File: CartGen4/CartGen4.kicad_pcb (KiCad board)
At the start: 4 copper layers, 52.8 x 60.9 mm, 77 parts, among them J1 MEM2080-00-128-00-A, SW1 SW_Push, U1 TPS65266-1RHBR, U10 IS25WP080D-JNLE, U11 DS1391U-33+, U2 SN74LV1T34DCKR, U3 SIT8008BI-73-33E-33.333333G, U4 NXS0108BQX, U5 AS1C8M16PL-70BIN, U6 NXS0108BQX, U7 NXS0108BQX, U8 NXS0104BQX, U9 LFXP2-8E-5MN132C, Y1 FC-135R 32.7680KA-E5

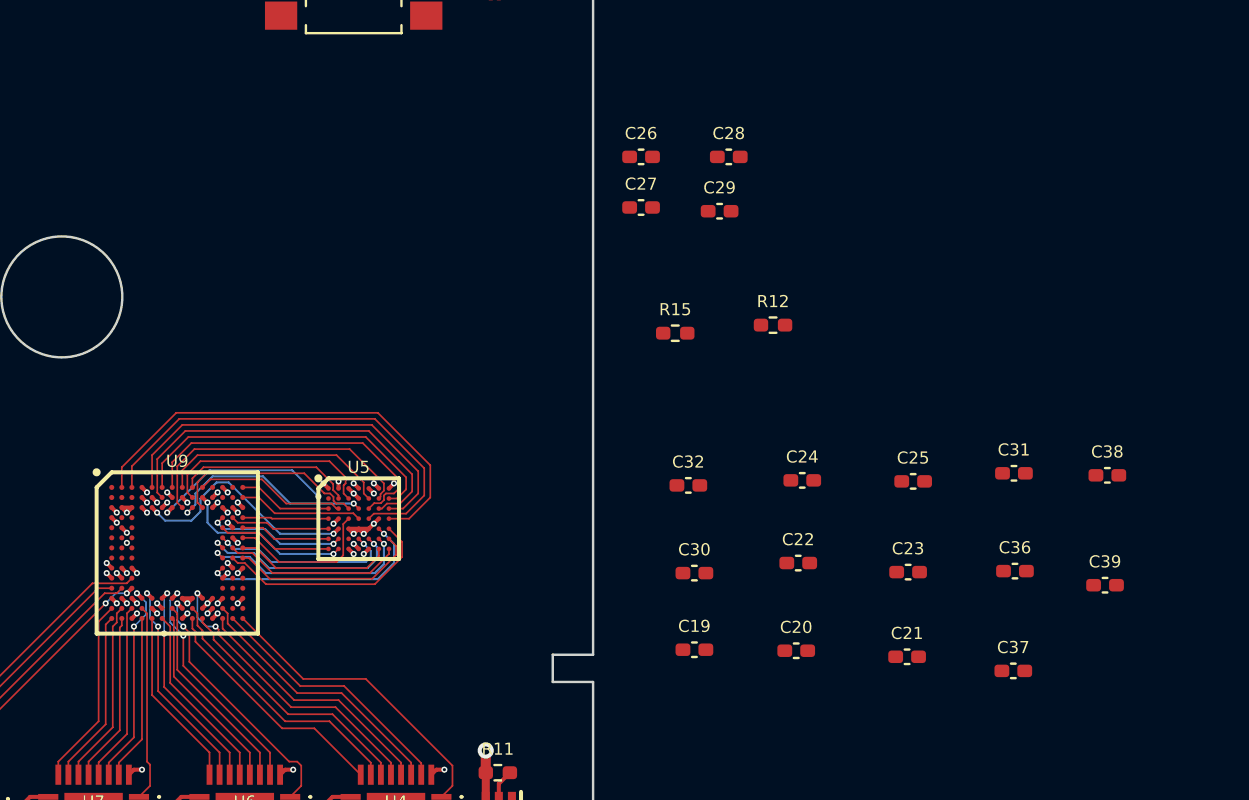
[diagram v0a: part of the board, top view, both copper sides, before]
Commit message: Added RAM decoupling capacitors
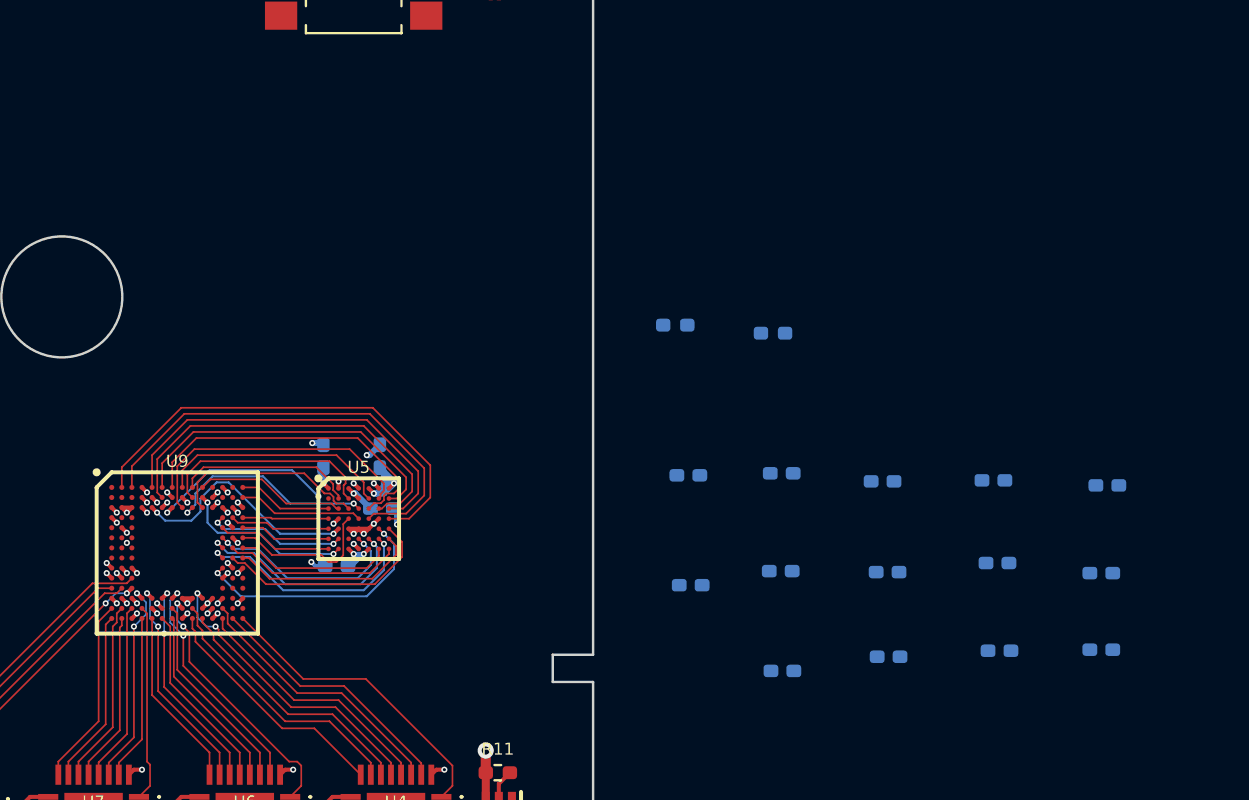
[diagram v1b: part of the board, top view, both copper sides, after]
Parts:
- C19, C20, C21, C22, C23, C24, C25, C26, C27, C28, C29, C30, C31, C32, C36, C37, C38, C39, R12, R15: moved to B.Cu
- moved C29 25.9 mm to (79.7, 74.3), turned to 180 degrees
- moved C28 22.8 mm to (81.8, 68.8), turned to 90 degrees
- moved C26 21.7 mm to (81.9, 71.5)
- moved C32 20.8 mm to (117.9, 70.3), turned to 180 degrees
- moved C38 20.8 mm to (97.1, 69.8), turned to 180 degrees
- moved C39 20.6 mm to (97.2, 75.2), turned to 180 degrees
- moved C19 20.2 mm to (117.6, 78.5), turned to 180 degrees
- moved C30 20.2 mm to (117.6, 74.7), turned to 180 degrees
- moved C27 20.0 mm to (79.0, 68.8), turned to 90 degrees
- moved C36 11.6 mm to (101.7, 74.5), turned to 180 degrees
- moved C31 11.5 mm to (101.7, 69.7), turned to 180 degrees
- moved C37 11.5 mm to (101.8, 79.5), turned to 180 degrees
- moved C20 10.1 mm to (112.5, 78.5), turned to 180 degrees
- moved C22 9.88 mm to (112.4, 74.2), turned to 180 degrees
- moved C24 9.48 mm to (112.2, 70.0), turned to 180 degrees
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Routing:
- net +1V8: track 20.9 -> 29.4 mm
- net GND: track 81.4 -> 84.4 mm, vias 48 -> 52
- net RAM_CE1#: track 10.1 -> 11.0 mm
- net RAM_CRE: track 9.12 -> 10.0 mm
- net RAM_LB#: track 10.6 -> 11.4 mm
- net RAM_UB#: track 11.6 -> 12.4 mm

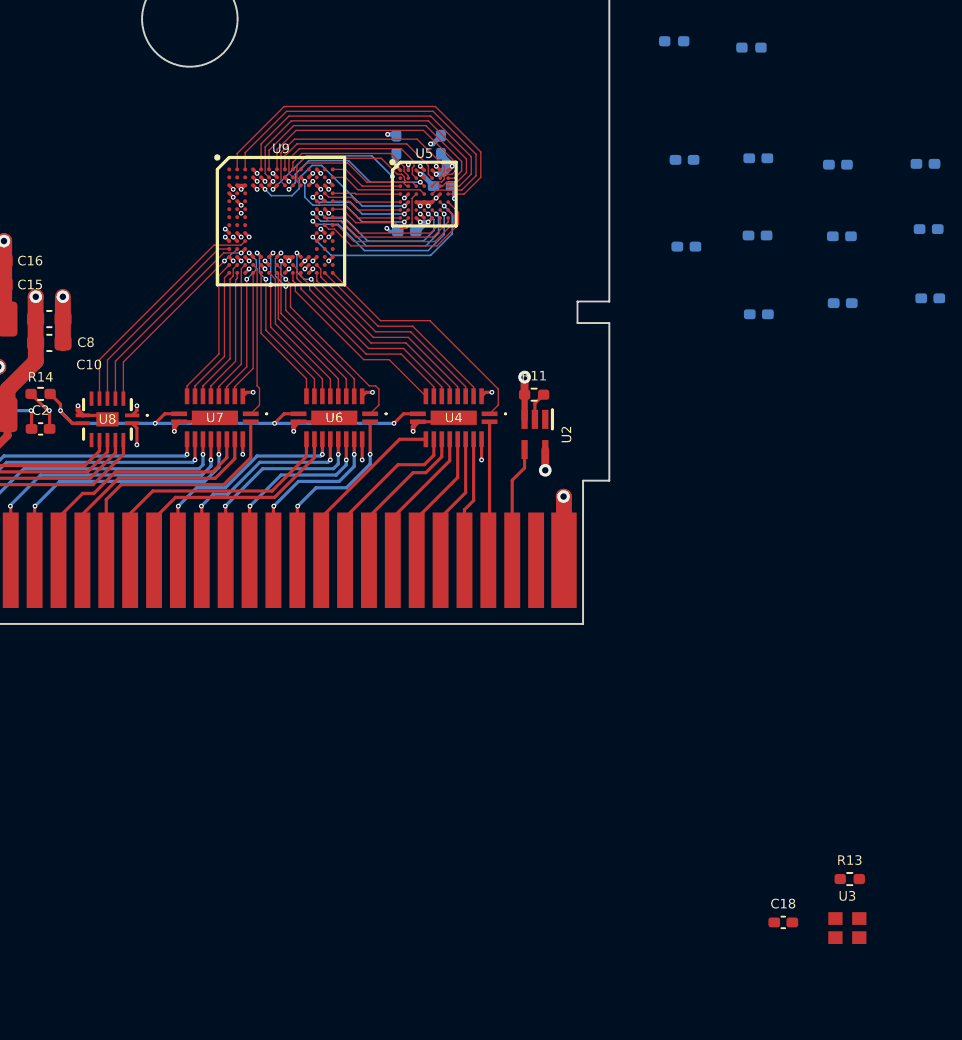
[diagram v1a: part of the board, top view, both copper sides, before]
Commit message: Connected FPGA ref clock
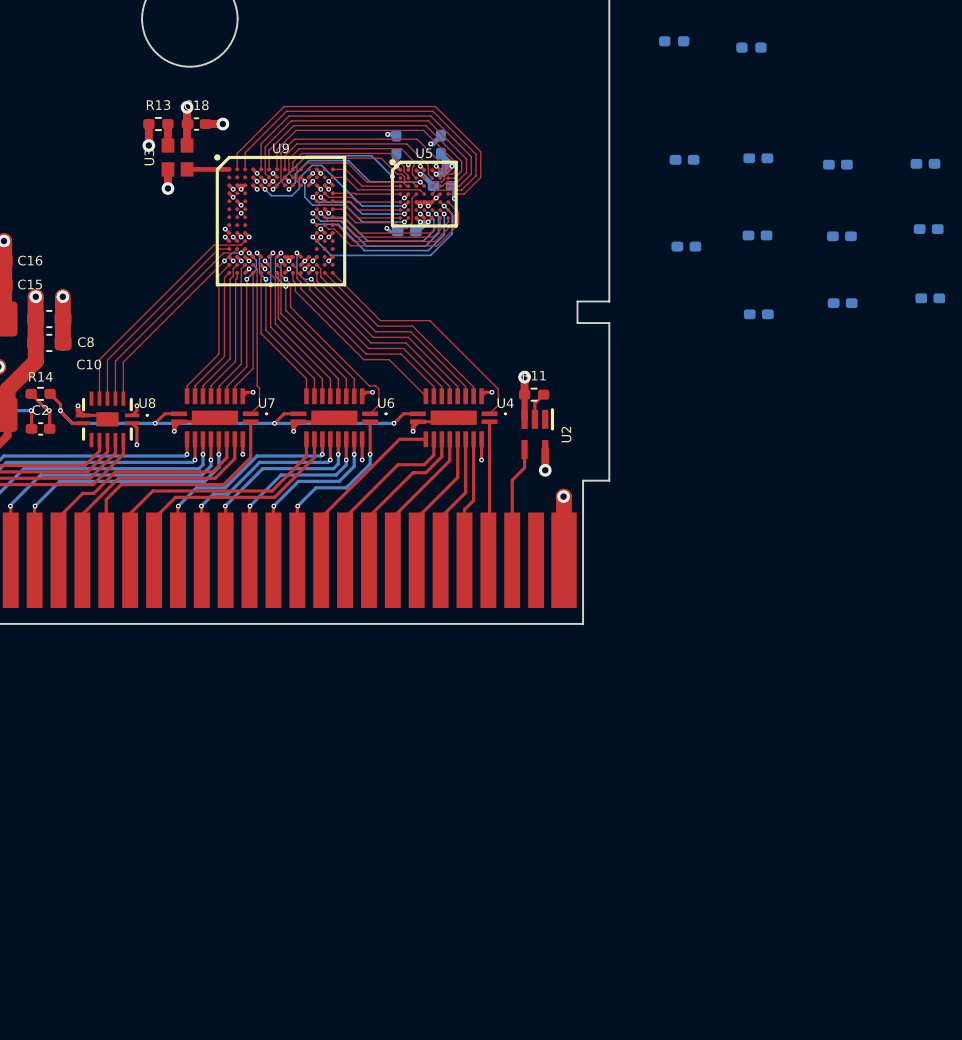
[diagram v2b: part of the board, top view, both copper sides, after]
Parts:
- moved R13 64.3 mm to (64.0, 67.5)
- moved U3 64.1 mm to (65.2, 69.7), turned to -90 degrees
- moved C18 62.2 mm to (66.5, 67.5)
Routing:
- net +1V8: track 29.4 -> 33.1 mm, vias 12 -> 14
- net FPGA_CLK33M: track 0.00 -> 2.65 mm
- net GND: track 84.4 -> 86.7 mm, vias 52 -> 54
- net Net-(R13-Pad2): track 0.00 -> 1.35 mm
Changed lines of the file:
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@@
   )
   (footprint "Resistor_SMD:R_0402_1005Metric_Pad0.72x0.64mm_HandSolder" (layer "F.Cu")
-    (at 107.475 114.975)
+    (at 64.05 67.55)
     (descr "Resistor SMD 0402 (1005 Metric), square (rectangular) end terminal, IPC_7351 nominal with elongated pad for handsoldering. (Body size source: IPC-SM-782 page 72, https://www.pcb-3d.com/wordpress/wp-content/uploads/ipc-sm-782a_amendment_1_and_2.pdf), generated with kicad-footprint-generator")
     (tags "resistor handsolder")
@@
   )
   (footprint "SamacSys_Parts:SIT8008BI-73-33E-33.333333G" (layer "F.Cu")
-    (at 107.325 118.055)
+    (at 65.25 69.65 -90)
     (property "Critical" "Y")
     (property "Description" "Standard Clock Oscillators -40 to 85C, 2016, 50ppm, 3.3V, 33.333333MHz, OE, 250 pcs T&R 8 mm")
@@
     (property "Source" "SPEC")
     (attr smd)
-    (fp_text reference "U3" (at 0 -2 unlocked) (layer "F.SilkS")
+    (fp_text reference "U3" (at 0 1.75 90 unlocked) (layer "F.SilkS")
       (effects (font (size 0.6 0.6) (thickness 0.125)))
     )
-    (fp_text value "SIT8008BI-73-33E-33.333333G" (at 0 -5.45 unlocked) (layer "F.Fab")
+    (fp_text value "SIT8008BI-73-33E-33.333333G" (at 0 -5.45 -90 unlocked) (layer "F.Fab") hide
       (effects (font (size 1 1) (thickness 0.15)))
     )
-    (fp_text user "${REFERENCE}" (at 0 -3.9 unlocked) (layer "F.Fab")
+    (fp_text user "${REFERENCE}" (at 0 -3.9 -90 unlocked) (layer "F.Fab") hide
       (effects (font (size 1 1) (thickness 0.15)))
     )
     (fp_rect (start -1 -0.8) (end 1 0.8) (layer "Dwgs.User") (width 0.05) (fill none))
     (fp_rect (start -1.5 -1.3) (end 1.5 1.3) (layer "F.CrtYd") (width 0.05) (fill none))
-    (pad "1" smd rect (at -0.75 0.6) (size 0.9 0.8) (layers "F.Cu" "F.Paste" "F.Mask")
+    (pad "1" smd rect (at -0.75 0.6 270) (size 0.9 0.8) (layers "F.Cu" "F.Paste" "F.Mask")
       (net 54 "Net-(R13-Pad2)") (pinfunction "OE") (pintype "input"))
-    (pad "2" smd rect (at 0.75 0.6) (size 0.9 0.8) (layers "F.Cu" "F.Paste" "F.Mask")
+    (pad "2" smd rect (at 0.75 0.6 270) (size 0.9 0.8) (layers "F.Cu" "F.Paste" "F.Mask")
       (net 24 "GND") (pinfunction "GND") (pintype "power_in"))
-    (pad "3" smd rect (at 0.75 -0.6) (size 0.9 0.8) (layers "F.Cu" "F.Paste" "F.Mask")
+    (pad "3" smd rect (at 0.75 -0.6 270) (size 0.9 0.8) (layers "F.Cu" "F.Paste" "F.Mask")
       (net 63 "FPGA_CLK33M") (pinfunction "OUT") (pintype "output"))
-    (pad "4" smd rect (at -0.75 -0.6) (size 0.9 0.8) (layers "F.Cu" "F.Paste" "F.Mask")
+    (pad "4" smd rect (at -0.75 -0.6 270) (size 0.9 0.8) (layers "F.Cu" "F.Paste" "F.Mask")
       (net 29 "+1V8") (pinfunction "VDD") (pintype "power_in"))
   )
@@
     (property "Source" "SPEC")
     (attr smd)
-    (fp_text reference "U7" (at 0 0) (layer "F.SilkS")
+    (fp_text reference "U7" (at -3.25 0.9) (layer "F.SilkS")
       (effects (font (size 0.6 0.6) (thickness 0.125)))
     )
@@
     (property "Source" "SPEC")
     (attr smd)
-    (fp_text reference "U6" (at 0 0) (layer "F.SilkS")
+    (fp_text reference "U6" (at -3.25 0.9) (layer "F.SilkS")
       (effects (font (size 0.6 0.6) (thickness 0.125)))
     )
@@
   )
   (footprint "Capacitor_SMD:C_0402_1005Metric_Pad0.74x0.62mm_HandSolder" (layer "F.Cu")
-    (at 103.3 117.7)
+    (at 66.45 67.55)
     (descr "Capacitor SMD 0402 (1005 Metric), square (rectangular) end terminal, IPC_7351 nominal with elongated pad for handsoldering. (Body size source: IPC-SM-782 page 76, https://www.pcb-3d.com/wordpress/wp-content/uploads/ipc-sm-782a_amendment_1_and_2.pdf), generated with kicad-footprint-generator")
     (tags "capacitor handsolder")
@@
     (property "Source" "SPEC")
     (attr smd)
-    (fp_text reference "U8" (at 0 0) (layer "F.SilkS")
+    (fp_text reference "U8" (at -2.5 1) (layer "F.SilkS")
       (effects (font (size 0.6 0.6) (thickness 0.125)))
     )
@@
     (property "Source" "SPEC")
     (attr smd)
-    (fp_text reference "U4" (at 0 0) (layer "F.SilkS")
+    (fp_text reference "U4" (at -3.25 0.9) (layer "F.SilkS")
       (effects (font (size 0.6 0.6) (thickness 0.125)))
     )
@@
   (segment (start 47.75 82.05) (end 47 82.8) (width 0.3) (layer "F.Cu") (net 24))
   (segment (start 81.75 71.95) (end 81.25 72.45) (width 0.2) (layer "F.Cu") (net 24))
+  (segment (start 68.1 67.55) (end 67.0175 67.55) (width 0.5) (layer "F.Cu") (net 24))
   (segment (start 51.75 74.9) (end 51.75 77.6) (width 1) (layer "F.Cu") (net 24))
   (segment (start 52.6375 76.15) (end 50.8625 76.15) (width 1) (layer "F.Cu") (net 24))
@@
   (segment (start 80.75 70.45) (end 80.5 70.2) (width 0.2) (layer "F.Cu") (net 24))
   (segment (start 52.6375 77.65) (end 52.6375 75.7875) (width 1) (layer "F.Cu") (net 24))
+  (segment (start 64.65 71.6) (end 64.65 70.4) (width 0.5) (layer "F.Cu") (net 24))
   (segment (start 65.05 86.85) (end 65.05 86.55) (width 0.3) (layer "F.Cu") (net 24))
   (segment (start 45.25 84.55) (end 47 82.8) (width 0.3) (layer "F.Cu") (net 24))
@@
   (via (at 68.75 72.15) (size 0.3024) (drill 0.15) (layers "F.Cu" "B.Cu") (net 24))
   (via (at 58.05 78.4) (size 0.8) (drill 0.4) (layers "F.Cu" "B.Cu") (free) (net 24))
+  (via (at 64.65 71.6) (size 0.8) (drill 0.4) (layers "F.Cu" "B.Cu") (free) (net 24))
   (via (at 89.5 90.95) (size 0.8) (drill 0.4) (layers "F.Cu" "B.Cu") (free) (net 24))
   (via (at 78.4 74.1) (size 0.3024) (drill 0.15) (layers "F.Cu" "B.Cu") (net 24))
@@
   (via (at 80.5 73.2) (size 0.3024) (drill 0.15) (layers "F.Cu" "B.Cu") (net 24))
   (via (at 69.25 72.65) (size 0.3024) (drill 0.15) (layers "F.Cu" "B.Cu") (net 24))
+  (via (at 68.1 67.55) (size 0.8) (drill 0.4) (layers "F.Cu" "B.Cu") (free) (net 24))
   (via (at 80.5 70.2) (size 0.3024) (drill 0.15) (layers "F.Cu" "B.Cu") (net 24))
   (via (at 68.25 74.65) (size 0.3024) (drill 0.15) (layers "F.Cu" "B.Cu") (net 24))
@@
   (segment (start 54.575 85.8) (end 54.575 84.225) (width 1) (layer "F.Cu") (net 29))
   (segment (start 74.750001 71.150001) (end 75 71.4) (width 0.2) (layer "F.Cu") (net 29))
+  (segment (start 65.85 68.9) (end 65.85 66.5) (width 0.5) (layer "F.Cu") (net 29))
   (segment (start 81.25 70.45) (end 81.5 70.7) (width 0.2) (layer "F.Cu") (net 29))
   (segment (start 54.575 87.125) (end 53.45 88.25) (width 0.5) (layer "F.Cu") (net 29))
   (segment (start 79 70.2) (end 79.25 70.45) (width 0.2) (layer "F.Cu") (net 29))
+  (segment (start 63.45 67.5525) (end 63.4525 67.55) (width 0.3) (layer "F.Cu") (net 29))
   (segment (start 56.3375 79.8) (end 56.3375 78.4125) (width 1) (layer "F.Cu") (net 29))
   (segment (start 54.575 84.225) (end 56.35 82.45) (width 1) (layer "F.Cu") (net 29))
@@
   (segment (start 56.3375 81.3) (end 56.3375 79.8) (width 1) (layer "F.Cu") (net 29))
   (segment (start 71.25 70.65) (end 71.5 70.9) (width 0.2) (layer "F.Cu") (net 29))
+  (segment (start 63.45 68.9) (end 63.45 67.5525) (width 0.5) (layer "F.Cu") (net 29))
   (segment (start 74.75 73.152341) (end 74.75 73.15) (width 0.2) (layer "F.Cu") (net 29))
   (segment (start 56.3375 78.4125) (end 56.35 78.4) (width 1) (layer "F.Cu") (net 29))
@@
   (via (at 82.5 70.2) (size 0.3024) (drill 0.15) (layers "F.Cu" "B.Cu") (net 29))
   (via (at 71.25 70.65) (size 0.3024) (drill 0.15) (layers "F.Cu" "B.Cu") (net 29))
+  (via (at 65.85 66.5) (size 0.8) (drill 0.4) (layers "F.Cu" "B.Cu") (free) (net 29))
   (via (at 79 70.2) (size 0.3024) (drill 0.15) (layers "F.Cu" "B.Cu") (net 29))
+  (via (at 63.45 68.9) (size 0.8) (drill 0.4) (layers "F.Cu" "B.Cu") (free) (net 29))
   (via (at 74.750001 71.147659) (size 0.3024) (drill 0.15) (layers "F.Cu" "B.Cu") (net 29))
   (via (at 80.5 70.7) (size 0.3024) (drill 0.15) (layers "F.Cu" "B.Cu") (net 29))
@@
   (segment (start 46.65 86) (end 46.75 85.9) (width 0.2) (layer "F.Cu") (net 53))
   (via (at 46.65 86) (size 0.3024) (drill 0.15) (layers "F.Cu" "B.Cu") (free) (net 53))
+  (segment (start 64.6475 68.8975) (end 64.65 68.9) (width 0.3) (layer "F.Cu") (net 54))
+  (segment (start 64.6475 67.55) (end 64.6475 68.8975) (width 0.5) (layer "F.Cu") (net 54))
   (segment (start 57.2475 84.5) (end 57.25 84.5) (width 0.2) (layer "F.Cu") (net 55))
   (segment (start 57.9 85.15) (end 57.9 85.55) (width 0.2) (layer "F.Cu") (net 55))
@@
   (segment (start 69 74.9) (end 68.75 74.65) (width 0.2) (layer "F.Cu") (net 56))
   (via (at 68.75 74.65) (size 0.3024) (drill 0.15) (layers "F.Cu" "B.Cu") (net 56))
+  (segment (start 68.5 70.4) (end 65.85 70.4) (width 0.3) (layer "F.Cu") (net 63))
   (segment (start 76.95 82.35) (end 78.55 82.35) (width 0.085) (layer "F.Cu") (net 64))
   (segment (start 72.65 77.55) (end 72.65 78.05) (width 0.085) (layer "F.Cu") (net 64))
